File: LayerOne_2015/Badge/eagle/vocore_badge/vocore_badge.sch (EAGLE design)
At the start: 17 parts

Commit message: edited holes.
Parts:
- R1, R10, R2, R3, R4, R5, R6, R7, R8, R9: value 0402_L -> (none); device vocore_dock:0402_L -> SparkFun-Resistors:RESISTOR0805-RES
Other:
- moved on the sheet: U$1

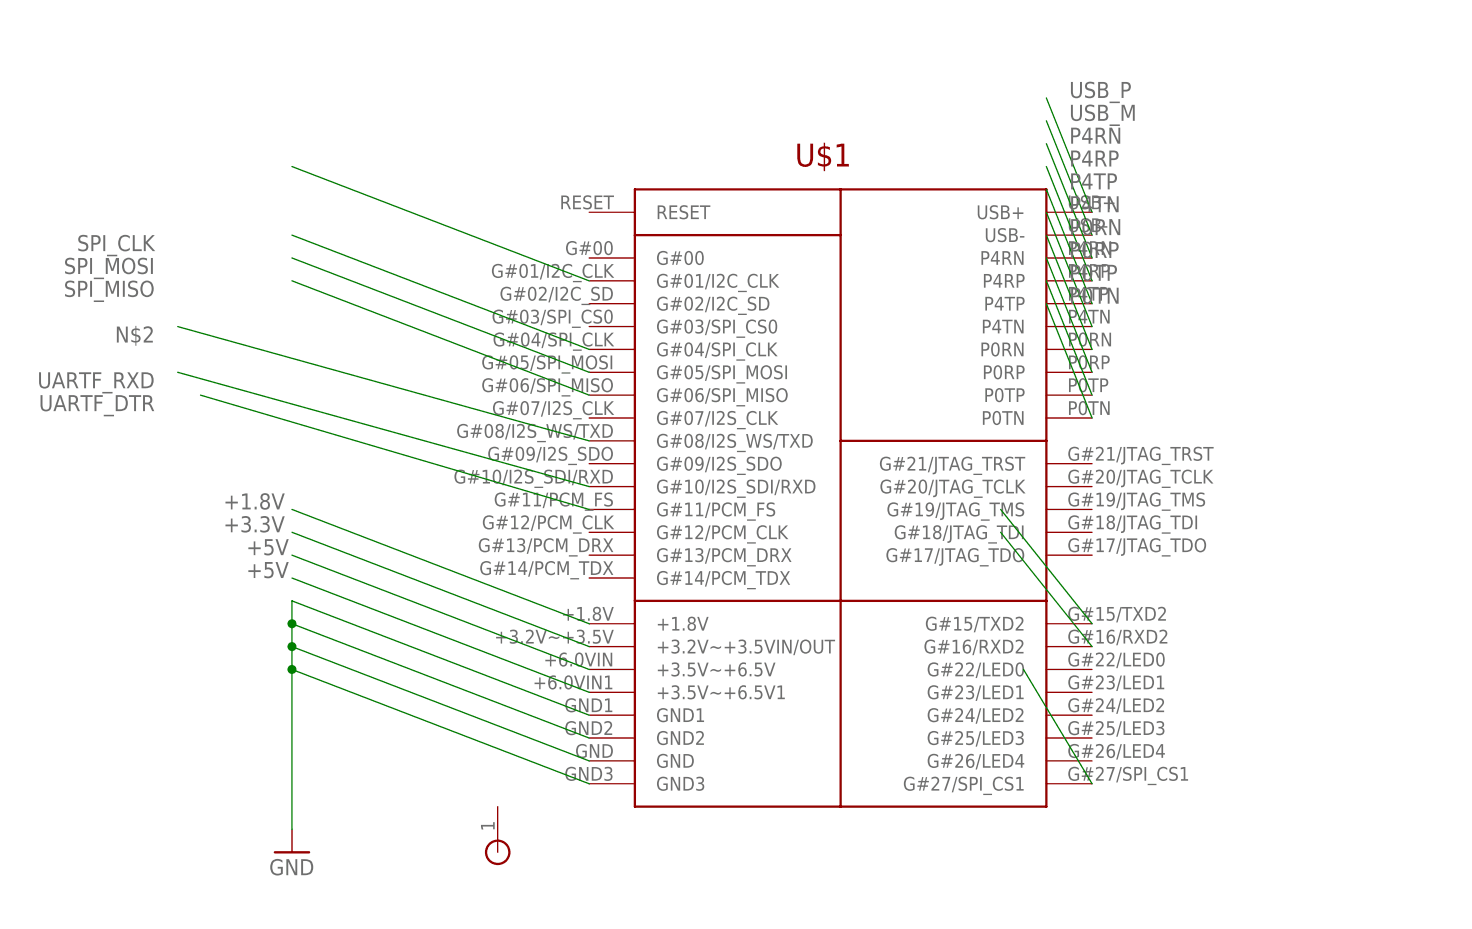
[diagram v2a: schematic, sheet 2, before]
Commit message: 
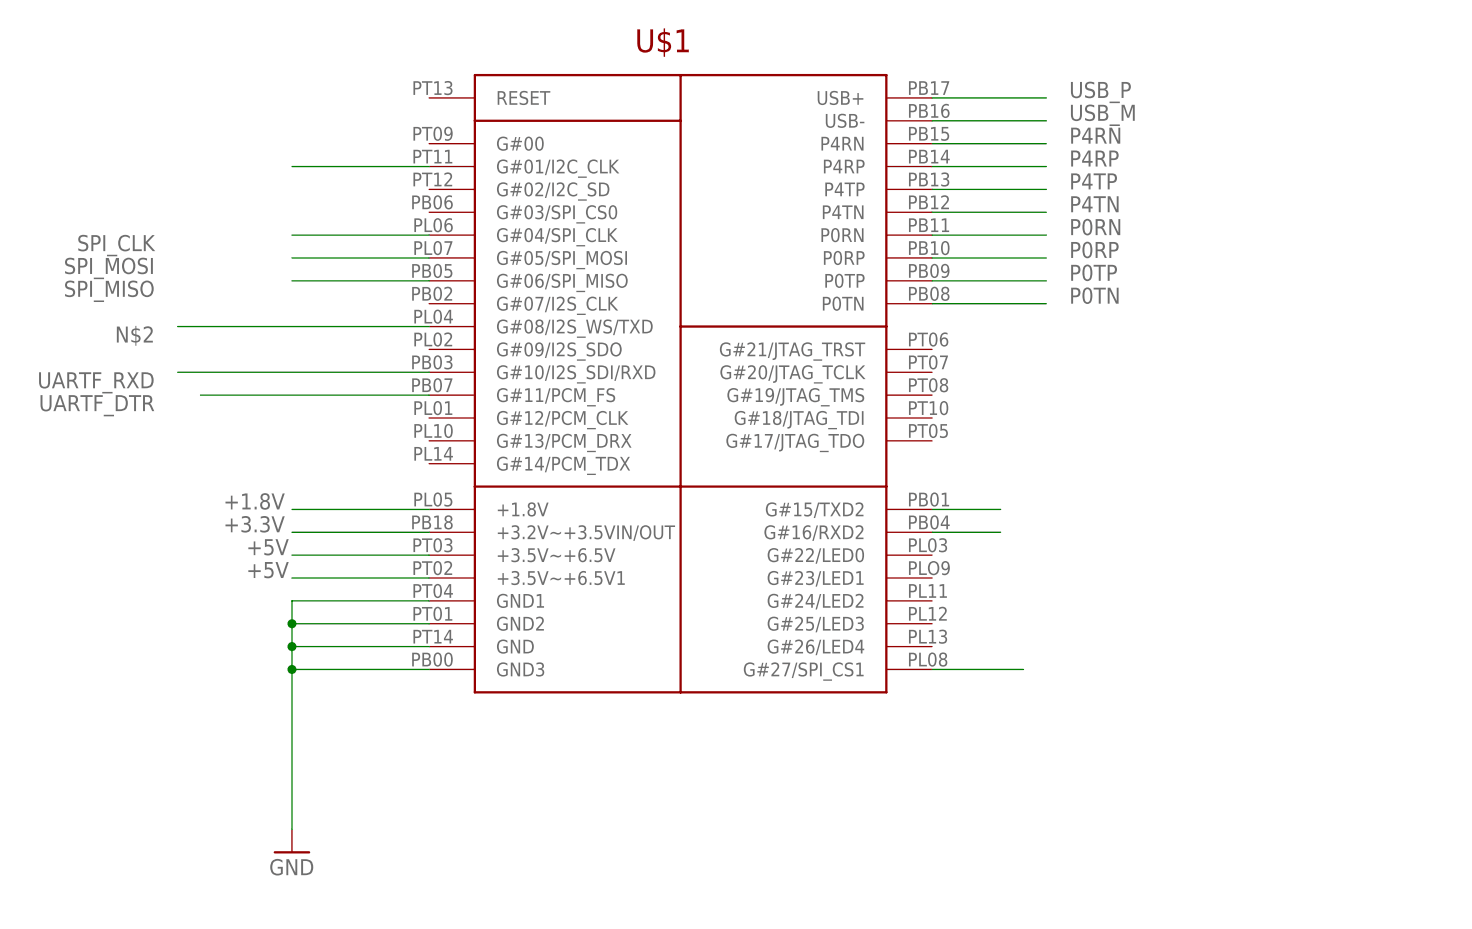
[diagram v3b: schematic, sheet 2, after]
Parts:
- removed PB06: PORT_1PIN, vocore_dock:PORT_1PIN
- removed USB2: USB_FULL_TALL, vocore_dock:USB_FULL_TALL
- added X1: (no value), con-amp:USB-787616
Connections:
- net +5V: now also X1.4; no longer USB2.VCC
- net GND: now also X1.1; no longer USB2.GND
- net USB_M: now also X1.3; no longer USB2.D-
- net USB_P: now also X1.2; no longer USB2.D+
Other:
- moved on the sheet: U$1

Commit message: 
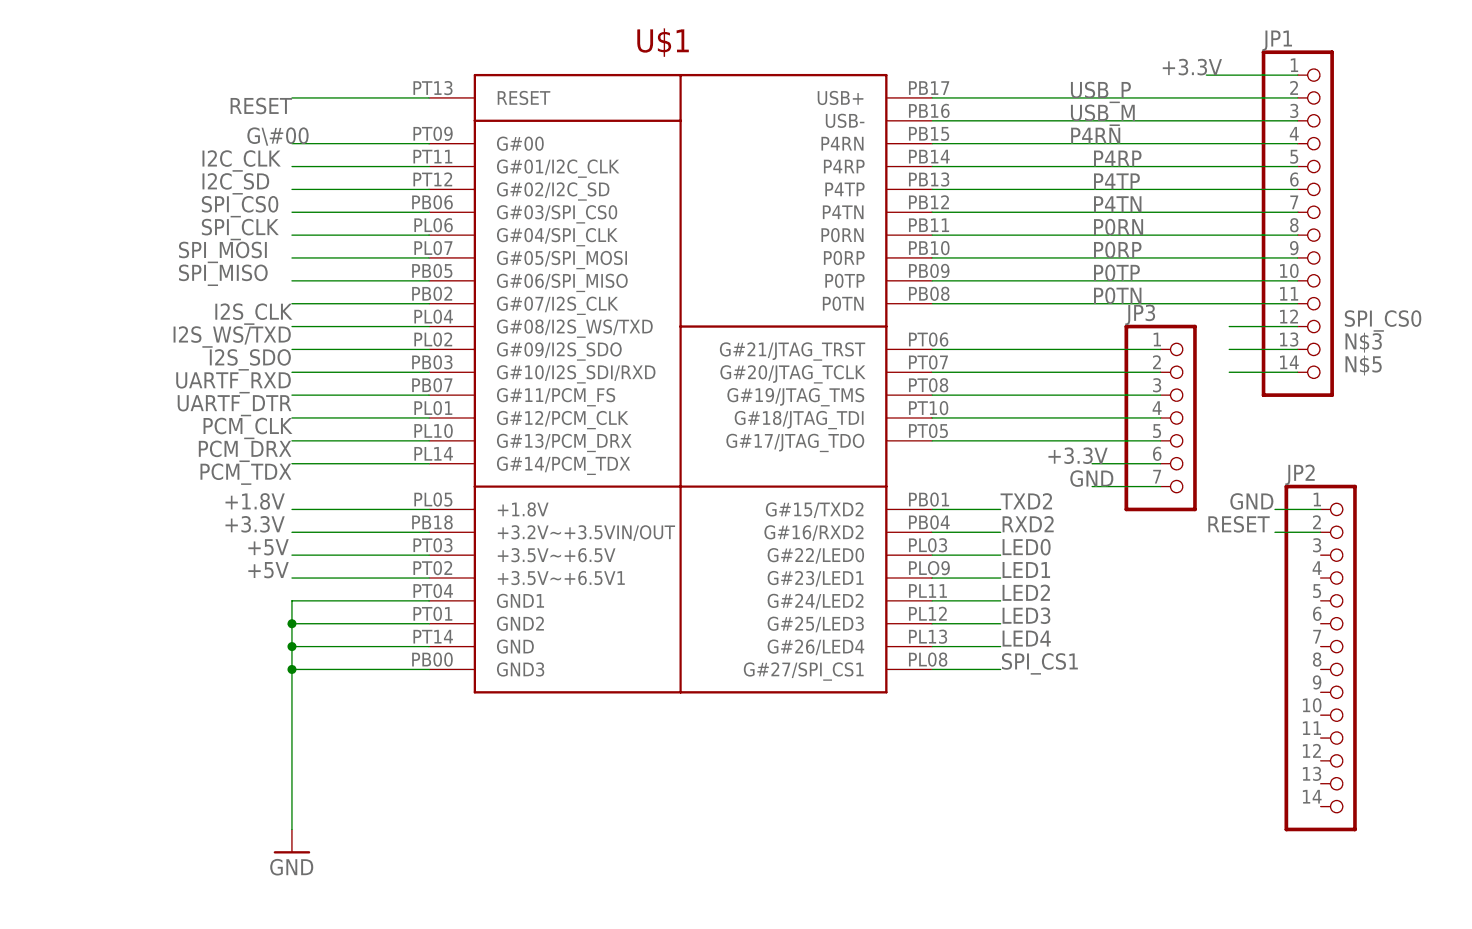
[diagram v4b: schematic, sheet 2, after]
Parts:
- added JP1, JP2: (no value), adafruit:PINHD-1X14
- added JP3: (no value), microbuilder:HEADER-1X7ROUND
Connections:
- net N$11 renamed I2C_CLK
- net N$12 renamed TXD2
- net N$13 renamed RXD2
- net N$2 renamed I2S_WS/TXD
- new net G\#00: U$1.G#00
- new net I2C_SD: U$1.G#02/I2C_SD
- new net I2S_CLK: U$1.G#07/I2S_CLK
- new net I2S_SDO: U$1.G#09/I2S_SDO
- new net JTAG_TCLK: JP3.2, U$1.G#20/JTAG_TCLK
- new net JTAG_TDI: JP3.4, U$1.G#18/JTAG_TDI
- new net JTAG_TDO: JP3.5, U$1.G#17/JTAG_TDO
- new net JTAG_TMS: JP3.3, U$1.G#19/JTAG_TMS
- new net JTAG_TRST: JP3.1, U$1.G#21/JTAG_TRST
- new net LED0: U$1.G#22/LED0
- new net LED1: U$1.G#23/LED1
- new net LED2: U$1.G#24/LED2
- new net LED3: U$1.G#25/LED3
- new net LED4: U$1.G#26/LED4
- new net N$3: JP1.13
- new net N$5: JP1.14
- new net PCM_CLK: U$1.G#12/PCM_CLK
- new net PCM_DRX: U$1.G#13/PCM_DRX
- new net PCM_TDX: U$1.G#14/PCM_TDX
- new net RESET: JP2.2, U$1.RESET
- new net SPI_CS0: JP1.12, U$1.G#03/SPI_CS0
- net +3.3V: now also JP1.1, JP3.6
- net GND: now also JP2.1, JP3.7
- net P0RN: now also JP1.8
- net P0RP: now also JP1.9
- net P0TN: now also JP1.11
- net P0TP: now also JP1.10
- net P4RN: now also JP1.4
- net P4RP: now also JP1.5
- net P4TN: now also JP1.7
- net P4TP: now also JP1.6
- net USB_M: now also JP1.3
- net USB_P: now also JP1.2
